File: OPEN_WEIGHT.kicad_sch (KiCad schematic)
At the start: 0 parts

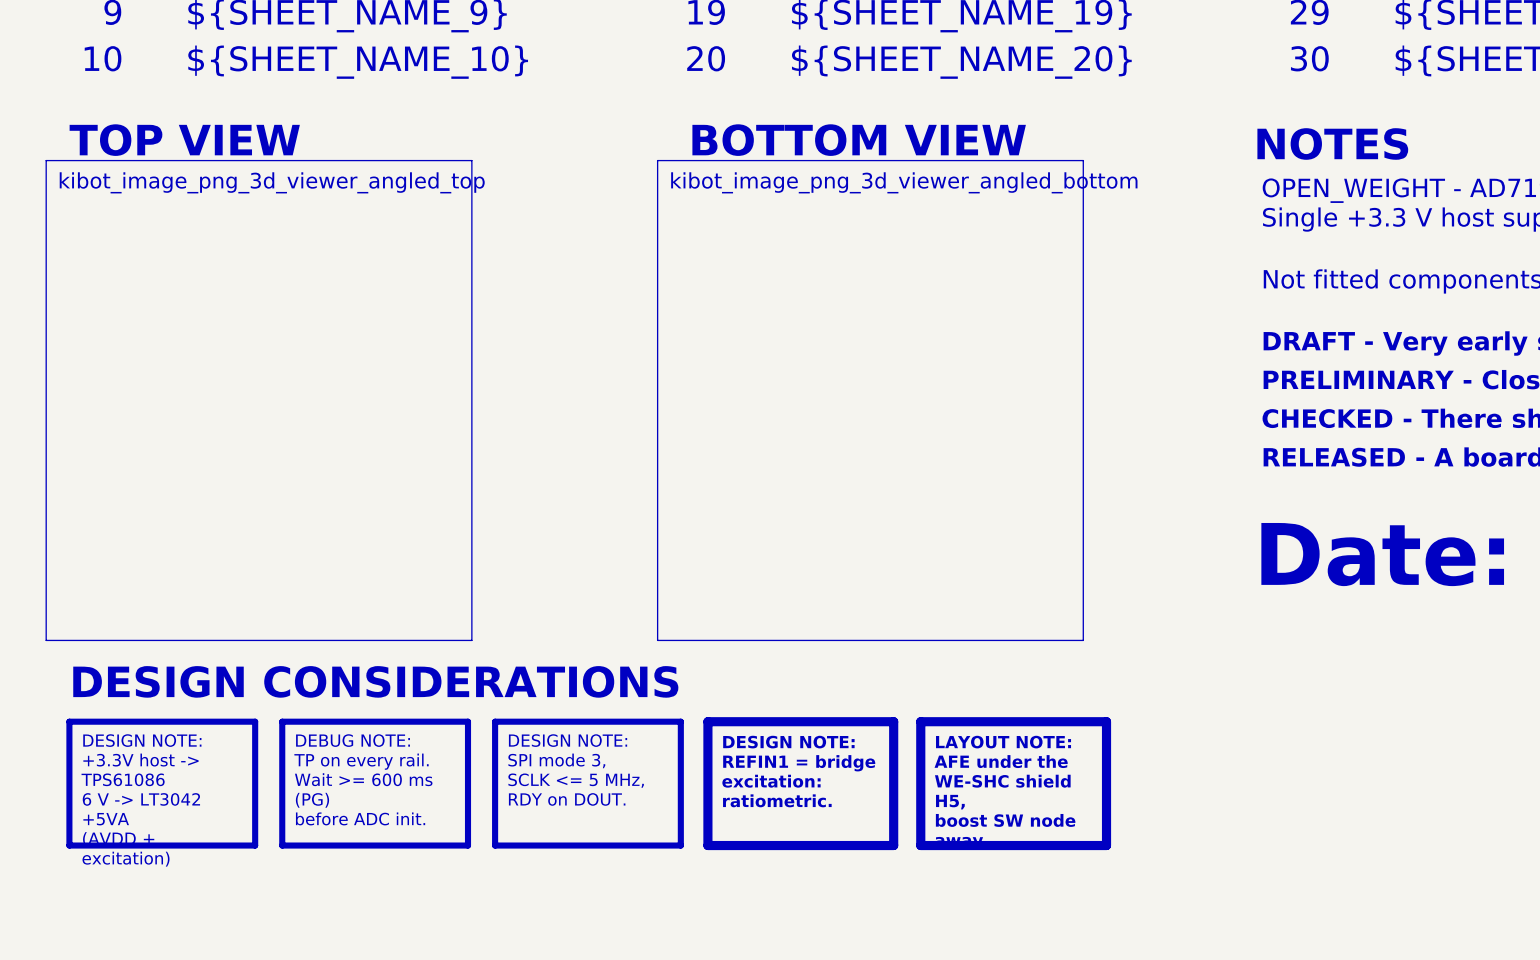
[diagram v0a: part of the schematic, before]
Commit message: Restyle the schematic like OPEN_PHASE, merge the power sheets, rework the bottom silkscreen
- Schematic: all sheets on A3 in the OPEN_PHASE look (red header bands,
  DESCRIPTION / DESIGN NOTE / LAYOUT NOTE / CALCULS & BUDGET panels in
  French, TEST POINTS panel, References in the title block)
- Title block: INGENIERIE FRANCE logo in KDT_Template_GIT.kicad_wks,
  per-sheet logo images removed
- Power - Sequencing rebuilt with curves from LTspice simulations 01-04
- TPS61086 and LT3042 sheets merged into Power Supply - Analog Rails
  (page 5, keeps the TPS sheet UUID); pages renumbered to 9, local nets
  renamed to /Project Architecture/Power_Supply/*, PCB links updated
- PCB: per-rail net colours (+3.3V, +6V, +5VA, GND) as on OPEN_PHASE
- PCB B.SilkS: test point pills with Arial Black knockout names, J1
  pinout cells, E+/E-/S+/S- tags on the M12 pads, CELL 1 / CELL 2 titles
  and a LOAD CELL wiring panel

Netlist connectivity, ERC (2 warnings) and copper DRC unchanged;
schematic parity clean.

Co-Authored-By: Claude Opus 5.5 <noreply@anthropic.com>
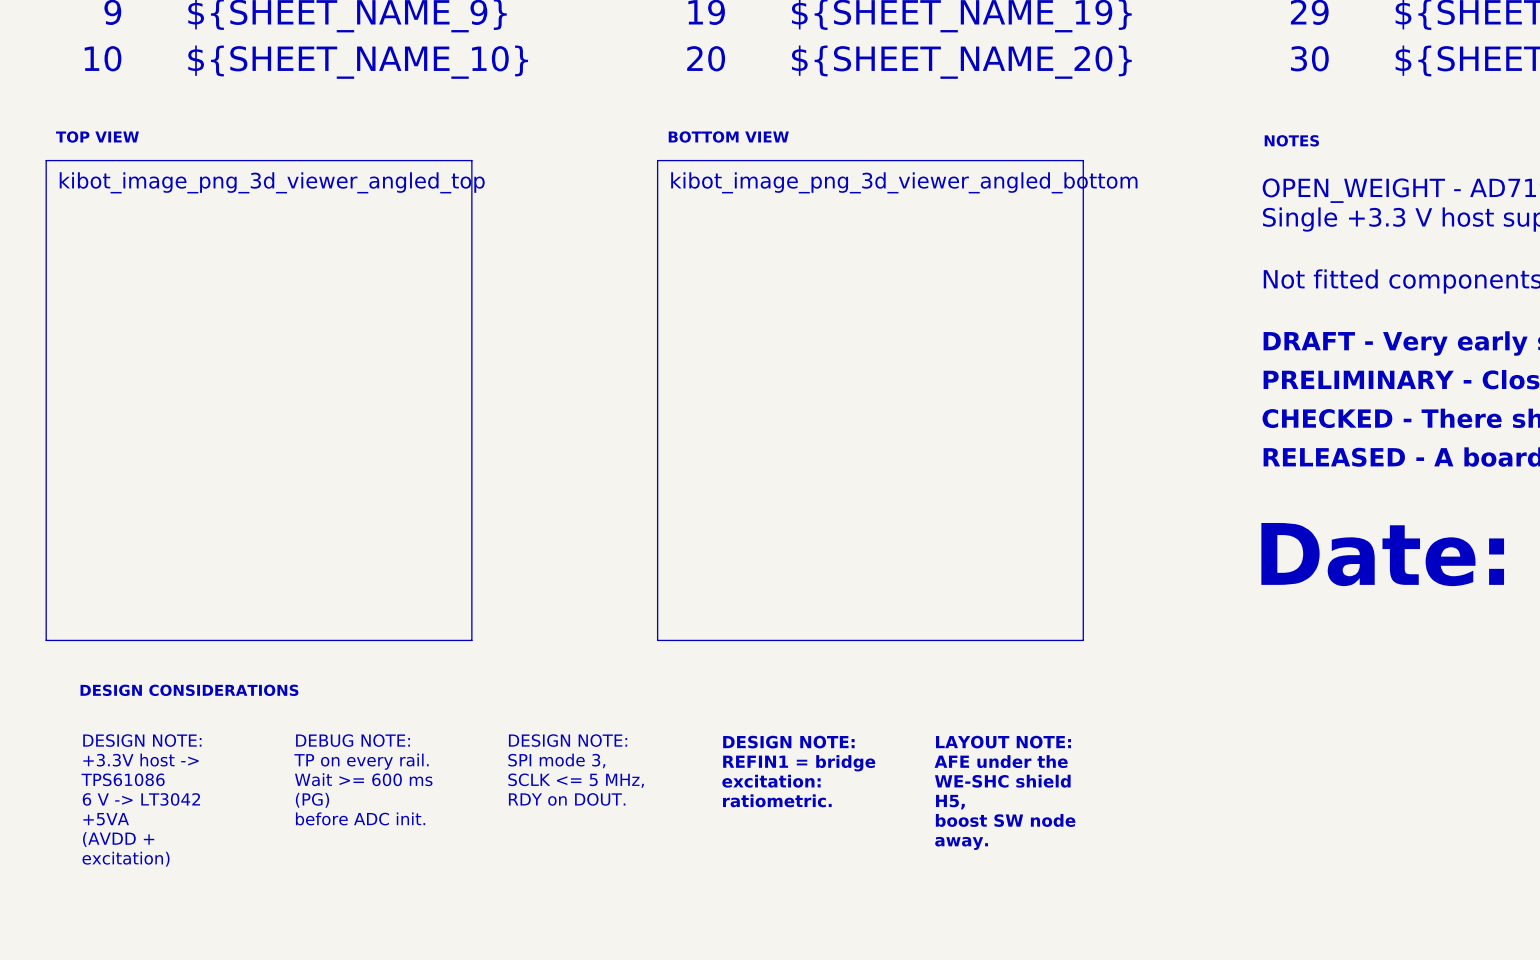
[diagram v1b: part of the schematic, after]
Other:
- note removed: "BOTTOM VIEW"
- note removed: "DESIGN CONSIDERATIONS"
- note removed: "NOTES"
- note removed: "TOP VIEW"
